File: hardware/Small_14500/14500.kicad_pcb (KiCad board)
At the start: 2 copper layers, 92.8 x 16 mm, 50 parts, among them J2 Battery, J3 GPIO, J4 USB_B_Micro, J5 Power, J6 LEDs, J7 GPIO, Q1 BSS806N, Q2 BSS806N, Q3 BSS806N, Q4 BSS806N, SW1 Mode, SW2 Power, U1 STM32L072KZUx, U2 AP2210N-3.3TRG1, U3 MCP73831T-2ACI_OT, U4 ESD7002WTT1G

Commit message: Rename "Mini" to "Small"
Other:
- board text added: "Small"
- board text removed: "Mini"
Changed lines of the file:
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@@
   (gr_arc (start 139.95 92) (end 138.85 92) (angle -180) (layer Edge.Cuts) (width 0.15))
   (gr_arc (start 139.95 108) (end 140.95 108) (angle -180) (layer Edge.Cuts) (width 0.15))
-  (gr_text Mini (at 120.575 94.65) (layer B.SilkS)
+  (gr_text Small (at 120.575 94.65) (layer B.SilkS)
     (effects (font (size 1.8 1.8) (thickness 0.15)) (justify left mirror))
   )

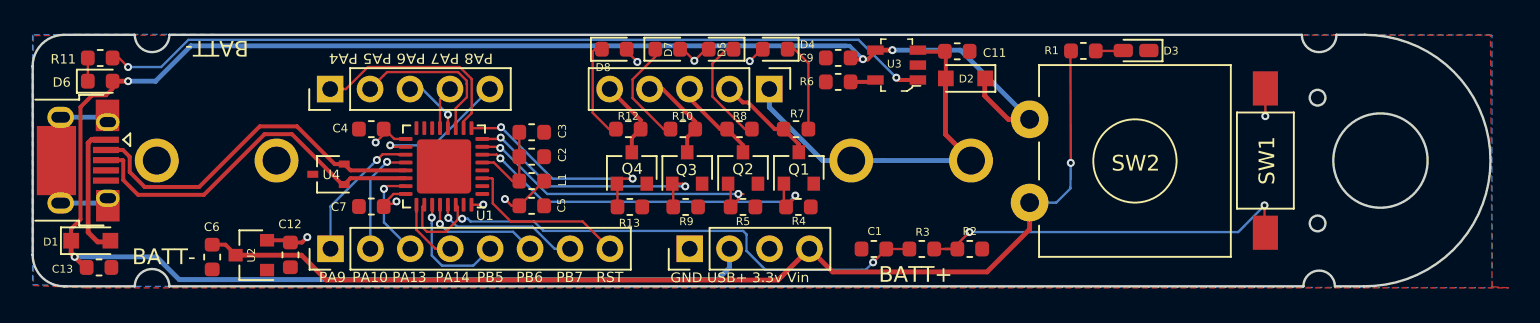
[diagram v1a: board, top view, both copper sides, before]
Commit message: Fix spacing around battery clips.
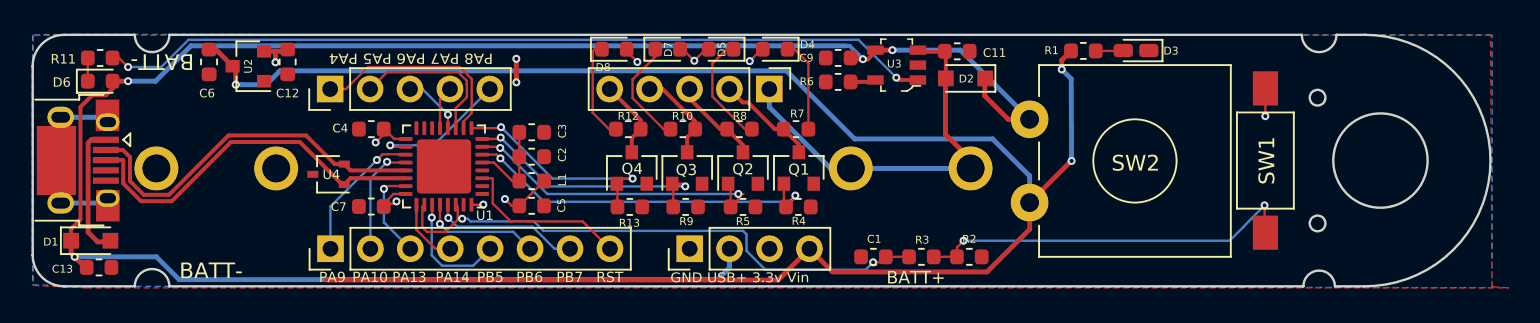
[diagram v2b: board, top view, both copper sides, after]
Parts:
- moved C6 12.4 mm to (69.3, 93.7)
- moved C12 12.3 mm to (74.3, 93.7)
- moved U2 12.0 mm to (71.8, 94.0)
- moved C1 0.50 mm to (111.6, 106.1)
- moved J2 0.50 mm to (91.9, 100.5)
- moved R2 0.50 mm to (117.7, 106.1)
- moved R3 0.50 mm to (114.6, 106.1)
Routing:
- net /VIN: track 68.9 -> 118.8 mm, vias 1 -> 3
- net +3V3: track 18.5 -> 19.5 mm, vias 9 -> 11
- net /BUTTON: track 37.2 -> 36.4 mm

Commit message: Update version number (1a2)
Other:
- board text added: "rev 1a2"
- board text removed: "rev 1"
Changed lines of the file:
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@@
   )
   (setup
-    (last_trace_width 0.31)
+    (last_trace_width 0.762)
     (user_trace_width 0.254)
     (user_trace_width 0.31)
@@
     (effects (font (size 1 1) (thickness 0.2)))
   )
-  (gr_text "rev 1" (at 137.3 96.5) (layer B.SilkS)
+  (gr_text "rev 1a2" (at 137.3 96.5) (layer B.SilkS)
     (effects (font (size 0.8 0.8) (thickness 0.1)) (justify left mirror))
   )

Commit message: Rename SCLK to SCK
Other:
- board text added: "SCK"
- board text removed: "SCLK"
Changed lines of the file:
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@@
   )
   (setup
-    (last_trace_width 0.762)
+    (last_trace_width 0.1524)
     (user_trace_width 0.254)
     (user_trace_width 0.31)
@@
     (effects (font (size 0.65 0.6) (thickness 0.1)) (justify mirror))
   )
-  (gr_text SCLK (at 79.57 93.6) (layer B.SilkS)
+  (gr_text SCK (at 79.57 93.6) (layer B.SilkS)
     (effects (font (size 0.65 0.6) (thickness 0.1)) (justify mirror))
   )
@@
   (gr_line (start 66.8 108) (end 138.95 108) (layer Edge.Cuts) (width 0.15))
   (gr_line (start 66.8 92) (end 138.85 92) (layer Edge.Cuts) (width 0.15))
-  (via (at 88.875 93.525) (size 0.508) (drill 0.254) (layers F.Cu B.Cu) (net 3))
-  (segment (start 88.875 93.525) (end 88.875 94.8) (width 0.31) (layer F.Cu) (net 3))
-  (via (at 88.875 95.025) (size 0.508) (drill 0.254) (layers F.Cu B.Cu) (net 3))
-  (segment (start 88.875 94.8) (end 88.875 95.025) (width 0.31) (layer F.Cu) (net 3))
   (segment (start 83.182602 104.532602) (end 84.38165 104.532602) (width 0.1524) (layer F.Cu) (net 1))
   (segment (start 85.145 103.769252) (end 85.145 102.9375) (width 0.1524) (layer F.Cu) (net 1))
@@
   (segment (start 62.575 102.705) (end 62.885 102.395) (width 0.31) (layer B.Cu) (net 2))
   (segment (start 59.885 102.705) (end 62.575 102.705) (width 0.31) (layer B.Cu) (net 2))
+  (via (at 88.875 93.525) (size 0.508) (drill 0.254) (layers F.Cu B.Cu) (net 3))
+  (segment (start 88.875 93.525) (end 88.875 94.8) (width 0.31) (layer F.Cu) (net 3))
+  (via (at 88.875 95.025) (size 0.508) (drill 0.254) (layers F.Cu B.Cu) (net 3))
+  (segment (start 88.875 94.8) (end 88.875 95.025) (width 0.31) (layer F.Cu) (net 3))
   (segment (start 81.1125 98.625) (end 80.4625 97.975) (width 0.1524) (layer F.Cu) (net 3))
   (segment (start 81.8325 98.625) (end 81.1125 98.625) (width 0.1524) (layer F.Cu) (net 3))

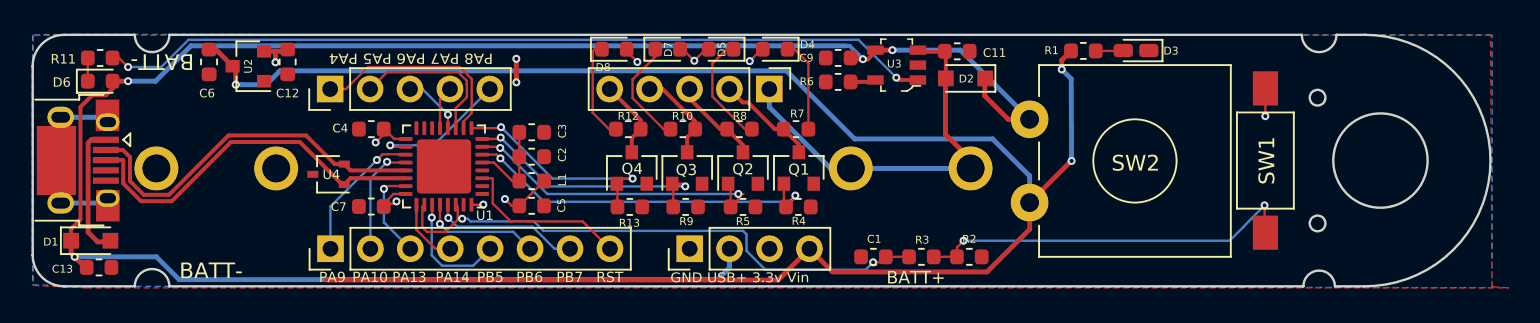
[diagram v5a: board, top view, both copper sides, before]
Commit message: Finish updating Small board with STM32F4
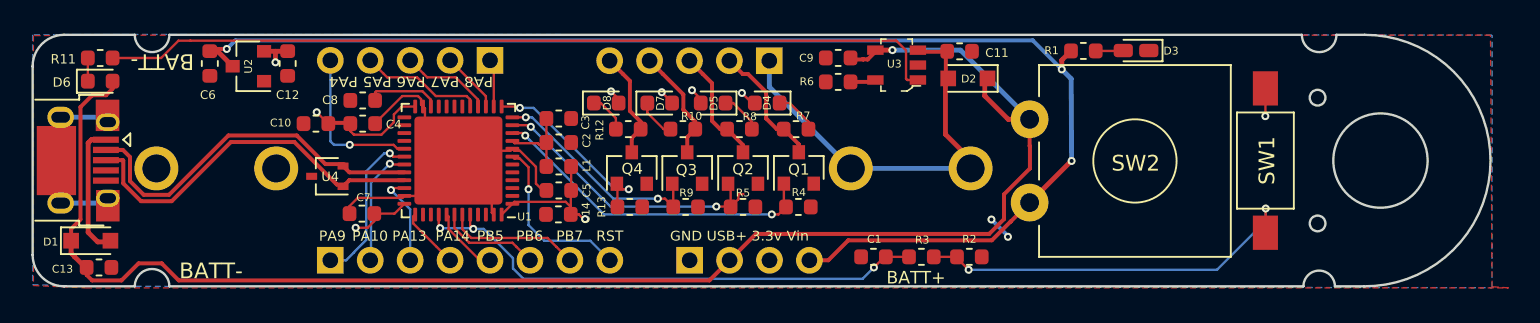
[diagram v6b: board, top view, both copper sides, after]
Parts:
- removed REF**: OSHW-Symbol_6.7x6mm_SilkScreen, Symbol:OSHW-Symbol_6.7x6mm_SilkScreen
- added C10: 100nf, Capacitor_SMD:C_0603_1608Metric, F.Cu at (76.1, 97.7)
- added C14: 100nf, Capacitor_SMD:C_0603_1608Metric, F.Cu at (91.5, 103.4)
- added C8: 4.7uF, Capacitor_SMD:C_0603_1608Metric, F.Cu at (79.1, 96.2)
- C3: value 10nf -> 100nf
- U1: value STM32L072KZUx -> STM32F412CGUx; footprint Package_DFN_QFN:QFN-32-1EP_5x5mm_P0.5mm_EP3.45x3.45mm -> Package_DFN_QFN:QFN-48-1EP_7x7mm_P0.5mm_EP5.6x5.6mm
- moved J3 10.3 mm to (87.2, 93.6), turned to 270 degrees
- moved D4 3.46 mm to (104.8, 96.3)
- moved D5 3.46 mm to (101.4, 96.3)
- moved D8 3.46 mm to (94.6, 96.3)
- moved D7 3.46 mm to (98.0, 96.3)
- moved C5 1.98 mm to (91.6, 101.9), turned to 180 degrees
- moved L1 1.96 mm to (91.6, 100.4)
- moved C2 1.95 mm to (91.6, 98.8)
- moved C3 1.93 mm to (91.6, 97.3)
- moved J6 1.81 mm to (105.0, 93.6)
- moved U1 0.99 mm to (85.2, 100.0)
- moved C7 0.75 mm to (79.0, 103.4)
- moved J7 0.74 mm to (77.0, 106.3)
- moved J5 0.73 mm to (99.9, 106.3)
- moved C4 0.65 mm to (79.1, 97.7), turned to 0 degrees
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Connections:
- J4 pad 4: Net-(J4-Pad4) -> (no net)
- U1 pad 1: Net-(U1-Pad1) -> +3V3
- U1 pad 10: /PA4 -> /LED1
- U1 pad 11: /PA5 -> /LED2
- U1 pad 12: /PA6 -> /LED3
- U1 pad 13: /PA7 -> /LED4
- U1 pad 14: Net-(U1-Pad14) -> /PA4
- U1 pad 15: Net-(U1-Pad15) -> /PA5
- U1 pad 16: GND -> /PA6
- U1 pad 17: +3V3 -> /PA7
- U1 pad 18: /PA8 -> (no net)
- U1 pad 19: /PA9 -> (no net)
- U1 pad 2: Net-(U1-Pad2) -> (no net)
- U1 pad 20: /PA10 -> (no net)
- U1 pad 21: /USB_D- -> (no net)
- U1 pad 22: /USB_D+ -> Net-(C8-Pad1)
- U1 pad 23: /PA13 -> GND
- U1 pad 25: /PA14 -> (no net)
- U1 pad 26: /BUTTON -> (no net)
- U1 pad 27: /PB5 -> (no net)
- U1 pad 28: /PB6 -> (no net)
- U1 pad 29: /PB7 -> /PA8
- U1 pad 3: /RESET -> (no net)
- U1 pad 30: /BUTTON -> /PA9
- U1 pad 31: GND -> /PA10
- U1 pad 32: +3V3 -> /USB_D-
- U1 pad 33: GND -> /USB_D+
- U1 pad 4: GND -> (no net)
- U1 pad 5: Net-(C2-Pad1) -> (no net)
- U1 pad 6: /LED1 -> (no net)
- U1 pad 7: /LED2 -> /RESET
- U1 pad 8: /LED3 -> GND
- U1 pad 9: /LED4 -> Net-(C2-Pad1)
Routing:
- net /VIN: track 118.8 -> 84.0 mm
- net GND: track 8.42 -> 39.1 mm, vias 0 -> 2
- net /VUSB: track 124.4 -> 100.2 mm, vias 4 -> 1
- net /PA4: track 13.2 -> 3.04 mm
- net +3V3: track 19.5 -> 29.7 mm, vias 11 -> 9
- net /PA5: track 10.1 -> 3.88 mm
- net /PA7: track 2.75 -> 7.83 mm
- net Net-(C8-Pad1): track 0.00 -> 4.72 mm
- net Net-(D5-Pad1): track 7.19 -> 2.64 mm
- net Net-(D7-Pad1): track 6.94 -> 2.53 mm
- net Net-(D8-Pad1): track 6.45 -> 2.50 mm
- net /PB5: track 7.66 -> 4.43 mm, vias 1 -> 0
- net Net-(D4-Pad1): track 5.89 -> 2.80 mm
- net /LED1: track 23.8 -> 21.3 mm
- net /LED3: track 16.6 -> 14.1 mm
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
